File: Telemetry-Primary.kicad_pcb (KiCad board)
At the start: 2 copper layers, 95 x 95 mm, 162 parts, among them J1 CAN_LogicAnalyzer, J10 SMAConn, J11 CAN_In, J12 CAN_Out, J13 Breakouts, J14 RTC_BATT, J2 IMU_LogicAnalyzer, J3 GPS_LogicAnalyzer, J4 SWD, J5 SDCard_LogicAnalyzer, J6 USB_B_Micro, J7 PowerConn, J8 RJ45_Abracon_ARJP11A-MASA-B-A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, J9 Micro_SD_Card_Det, Q1 Q_PMOS_GSD, SW1 Reset, SW2 RTCC_BattCheck, SW4 SW_Push, SW5 SW_Push, SW6 SW_Push, SW7 SW_Push, U1 STM32F429ZITx, U10 LAN8742A-CZ-TR, U11 USBLC6-4SC6, U2 RI3-1205S, U3 LD1117-3.3_SOT223, U4 ADM3055E, U5 CDSOT23-T24CAN, U6 BNO055, U7 MTK3339, U8 CP2102N-A02-GQFN24, U9 BLUENRG-M2SA, Y1 8M, Y2 25M, Y3 32.768k

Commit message: layout changes, telemetryCAN added, IMU removed
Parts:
- removed R1, R2: 4.7k, Resistor_SMD:R_0805_2012Metric
- removed R30: 10k, Resistor_SMD:R_0805_2012Metric
- added C65: 10u, Capacitor_SMD:C_0805_2012Metric, B.Cu at (150.4, 71.3)
- added C66: 0.1u, Capacitor_SMD:C_0805_2012Metric, B.Cu at (150.4, 68.8)
- added C67: 0.1u, Capacitor_SMD:C_0805_2012Metric, B.Cu at (150.4, 66.3)
- added C68: 0.01u, Capacitor_SMD:C_0805_2012Metric, B.Cu at (150.4, 63.9)
- added J15: CAN_Out, UTSVT_Connectors:Molex_MicroFit3.0_1x4xP3.00mm_PolarizingPeg_Vertical, F.Cu at (155.3, 49.4)
- added L3: 2k, Inductor_SMD:L_0805_2012Metric, F.Cu at (150.2, 52.7)
- added L4: 2k, Inductor_SMD:L_0805_2012Metric, F.Cu at (150.1, 57.3)
- added TP8: CAN_H, TestPoint:TestPoint_Keystone_5005-5009_Compact, F.Cu at (167.0, 60.5)
- added TP9: CAN_L, TestPoint:TestPoint_Keystone_5005-5009_Compact, F.Cu at (167.0, 54.9)
- added U12: ADM3055E, UTSVT_ICs:SOIC-20W_7.5x15.4mm_Pitch1.27mm, F.Cu at (154.6, 64.5)
- C36: value 6.8n -> 0.22u
- C37: value 120n -> 10u
- C39: value 0.1u -> 0.01u
- C42, C43, C44, C45, R35: moved to B.Cu
- J13: footprint Connector_PinHeader_2.54mm:PinHeader_1x06_P2.54mm_Vertical -> Connector_Molex:Molex_Micro-Fit_3.0_43045-0612_2x03_P3.00mm_Vertical
- J2: value IMU_LogicAnalyzer -> CAN_LogicAnalyzer; footprint Connector_PinHeader_2.54mm:PinHeader_1x05_P2.54mm_Vertical -> Connector_PinHeader_2.54mm:PinHeader_1x03_P2.54mm_Vertical
- LOGO2: moved to F.Cu
- R28: value 10k -> 0
- R29: value 10k -> 120; moved to B.Cu
- U6: value BNO055 -> CDSOT23-T24CAN; footprint Package_LGA:LGA-28_5.2x3.8mm_P0.5mm -> Package_TO_SOT_SMD:SOT-23W
- moved H2 117.2 mm to (181.3, 134.9)
- moved J10 83.7 mm to (111.6, 132.5), turned to 90 degrees
- moved U7 77.2 mm to (161.8, 127.6), turned to -90 degrees
- moved U9 68.9 mm to (177.2, 52.9), turned to -90 degrees
- moved C63 67.3 mm to (172.8, 48.3), turned to -90 degrees
- moved D4 67.0 mm to (151.3, 128.4), turned to 90 degrees
- moved R31 65.0 mm to (178.8, 63.4), turned to 180 degrees
- moved C62 63.9 mm to (169.7, 48.3), turned to -90 degrees
- moved R27 63.3 mm to (151.3, 124.4)
- moved C51 59.8 mm to (174.9, 63.4), turned to 180 degrees
- moved R3 56.6 mm to (116.0, 87.2), turned to 0 degrees
- moved D2 55.3 mm to (116.0, 89.6), turned to 180 degrees
- moved R34 54.5 mm to (144.3, 57.3), turned to 0 degrees
- moved TP7 53.6 mm to (127.1, 63.2)
- moved U5 53.2 mm to (139.1, 54.7), turned to 90 degrees
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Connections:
- net /CAN/CAN_H renamed /CarCAN/CAN_H
- net /CAN/CAN_L renamed /CarCAN/CAN_L
- net /CAN/RSlope renamed /CarCAN/RSlope
- net /USART7_TX renamed /USART6_RX
- C36 pad 1: +3.3V -> Net-(U12-V_ISO_Out)
- C36 pad 2: GND -> Net-(C36-Pad2)
- C37 pad 1: +3.3V -> Net-(J15-5V)
- C37 pad 2: GND -> Net-(J15-GND)
- C38 pad 1: GND -> Net-(J15-5V)
- C38 pad 2: Net-(U6-CAP) -> Net-(J15-GND)
- C39 pad 1: +3.3V -> Net-(J15-5V)
- C39 pad 2: GND -> Net-(J15-GND)
- J13 pad 2: /SPI3_CLK -> /SPI3_MISO
- J13 pad 3: /SPI3_MISO -> /PD0
- J13 pad 4: /SPI3_MOSI -> /SPI3_CLK
- J13 pad 5: /PD0 -> /SPI3_MOSI
- J2 pad 2: /I2C1_SCL -> /CAN2_TX
- J2 pad 3: /I2C1_SDA -> /CAN2_RX
- J3 pad 2: /USART2_TX -> /USART3_TX
- J3 pad 3: /USART2_RX -> /USART3_RX
- J3 pad 4: /PD7 -> /PD10
- J3 pad 5: /PG9 -> /PD11
- R27 pad 1: /PD7 -> /PD10
- R28 pad 1: +3.3V -> /TelemetryCAN/RSlope
- R28 pad 2: /PB5 -> Net-(J15-GND)
- R29 pad 1: GND -> /TelemetryCAN/CAN_H
- R29 pad 2: Net-(U6-COM3) -> /TelemetryCAN/CAN_L
- U1 pad 135: /PB5 -> /CAN2_RX
- U1 pad 136: /I2C1_SCL -> /CAN2_TX
- U1 pad 137: /I2C1_SDA -> /PB7
- U6 pad 1: unconnected-(U6-PIN1-Pad1) -> /TelemetryCAN/CAN_H
- U6 pad 2: GND -> /TelemetryCAN/CAN_L
- U6 pad 3: +3.3V -> Net-(J15-GND)
- U7 pad 10: /USART2_TX -> /USART3_TX
- U7 pad 13: /PG9 -> /PD11
- U7 pad 5: /PD7 -> /PD10
- U7 pad 9: /USART2_RX -> /USART3_RX
- U9 pad 10: /USART3_RX -> /USART2_RX
- U9 pad 11: /USART3_TX -> /USART2_TX
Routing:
- net +BATT: track 48.6 -> 154.8 mm, vias 1 -> 2
- net /PD11: track 0.00 -> 53.9 mm
- net /PD10: track 0.00 -> 47.1 mm
- net +3.3V: track 382.4 -> 342.0 mm
- net /PG9: track 36.7 -> 0.00 mm
- net Net-(J15-GND): track 0.00 -> 36.1 mm
- net /TelemetryCAN/CAN_H: track 0.00 -> 33.8 mm
- net /PD7: track 29.0 -> 0.00 mm
- net /I2C1_SCL: track 28.3 -> 0.00 mm, vias 2 -> 0
- net /PB4: track 26.7 -> 0.00 mm, vias 2 -> 0
- net /I2C1_SDA: track 24.7 -> 0.00 mm, vias 2 -> 0
- net /PB5: track 24.1 -> 0.00 mm, vias 2 -> 0
- net /CarCAN/CAN_L: track 70.1 -> 47.3 mm, vias 2 -> 0
- net /TelemetryCAN/CAN_L: track 0.00 -> 22.8 mm
- net Net-(J10-In): track 23.3 -> 45.6 mm
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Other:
- board size 95 x 95 mm -> 77.5 x 91.8 mm
- board text added: "+"
- board text added: "D10"
- board text added: "D11"
- board text added: "Jump if end of CarCAN"
- board text added: "RTC Check"
- board text added: "UTSVT - Telemetry Leader v3.0 Summer 2023 -Design by Sijin Woo, Chase Block, Andrew Nguyen"
- board text removed: "B4"
- board text removed: "B5"
- board text removed: "D7"
- board text removed: "G9"
- board text removed: "RTC Battery Check"
- board text removed: "SCL"
- board text removed: "SDA"
- board text removed: "UTSVT - Telemetry Leader v2.2 Summer 2023 Design by Sijin Woo and Chase Block"

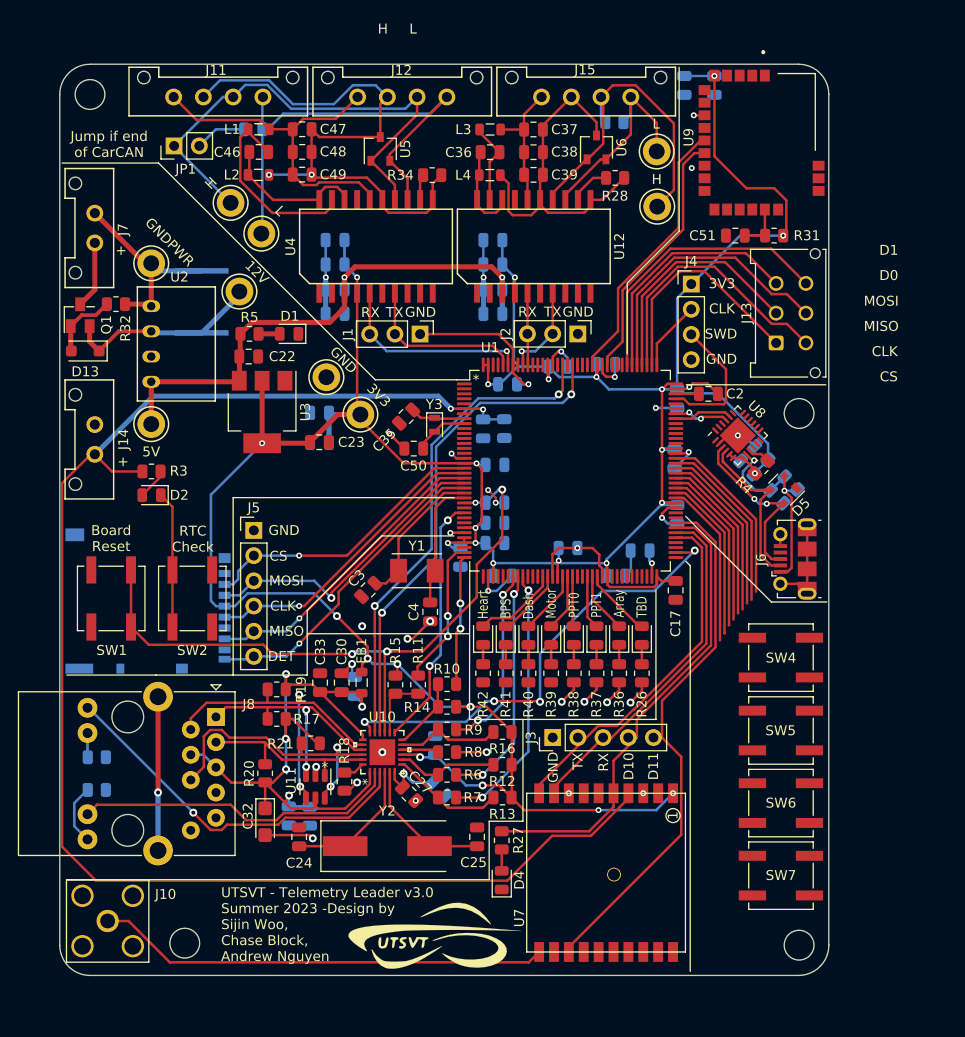
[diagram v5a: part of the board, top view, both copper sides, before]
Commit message: inputs routing + fixed models + clock keepouts
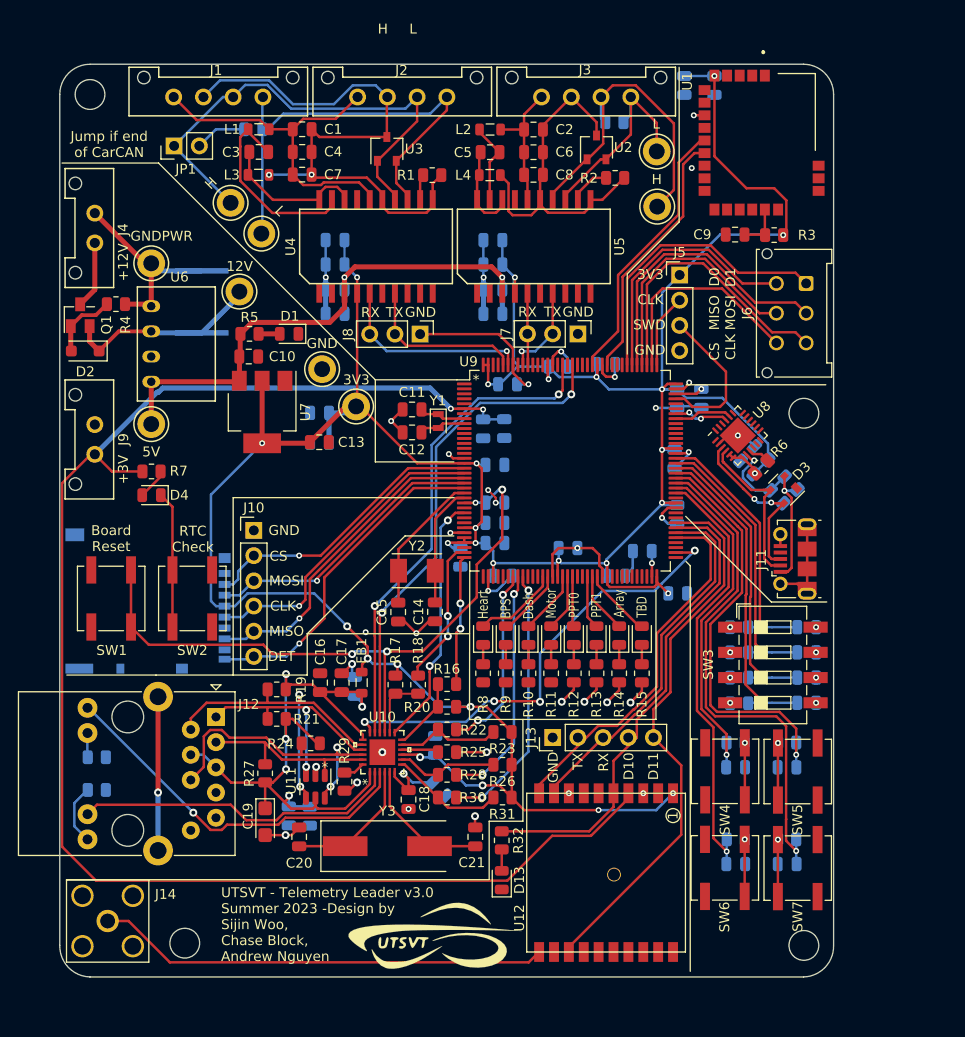
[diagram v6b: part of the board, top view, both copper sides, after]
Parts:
- added C56: .1u, Capacitor_SMD:C_0805_2012Metric, B.Cu at (182.1, 102.9)
- added C57: .1u, Capacitor_SMD:C_0805_2012Metric, B.Cu at (182.1, 105.4)
- added C58: .1u, Capacitor_SMD:C_0805_2012Metric, B.Cu at (182.1, 108.0)
- added C60: .1u, Capacitor_SMD:C_0805_2012Metric, B.Cu at (182.1, 110.5)
- added C62: .1u, Capacitor_SMD:C_0805_2012Metric, B.Cu at (180.1, 117.0)
- added C63: .1u, Capacitor_SMD:C_0805_2012Metric, B.Cu at (174.9, 117.0)
- added C67: .1u, Capacitor_SMD:C_0805_2012Metric, B.Cu at (180.1, 126.7)
- added C68: .1u, Capacitor_SMD:C_0805_2012Metric, B.Cu at (174.9, 126.7)
- added R37: 1k, Resistor_SMD:R_0805_2012Metric, B.Cu at (175.3, 102.9)
- added R38: 1k, Resistor_SMD:R_0805_2012Metric, B.Cu at (175.3, 105.4)
- added R39: 1k, Resistor_SMD:R_0805_2012Metric, B.Cu at (175.3, 108.0)
- added R40: 1k, Resistor_SMD:R_0805_2012Metric, B.Cu at (175.3, 110.5)
- added R41: 1k, Resistor_SMD:R_0805_2012Metric, B.Cu at (180.1, 114.5)
- added R42: 1k, Resistor_SMD:R_0805_2012Metric, B.Cu at (174.9, 114.5)
- added R45: 1k, Resistor_SMD:R_0805_2012Metric, B.Cu at (180.1, 124.3)
- added R46: 1k, Resistor_SMD:R_0805_2012Metric, B.Cu at (174.9, 124.3)
- added SW3: SW_DIP_x04, Button_Switch_SMD:SW_DIP_SPSTx04_Slide_6.7x11.72mm_W8.61mm_P2.54mm_LowProfile, F.Cu at (178.7, 106.7)
- C36: renamed from C2; moved to B.Cu
- C55: renamed from C17; moved to B.Cu
- moved SW5 11.6 mm to (181.2, 117.4), turned to -90 degrees
- moved LOGO2 9.33 mm to (157.5, 121.7)
- moved SW4 6.98 mm to (173.8, 117.4), turned to 90 degrees
- moved SW7 6.77 mm to (181.2, 127.2), turned to -90 degrees
- moved J6 6.72 mm to (182.0, 68.2), turned to -90 degrees
- moved SW6 5.71 mm to (173.8, 127.1), turned to 90 degrees
- moved C15 3.76 mm to (140.9, 101.3), turned to -90 degrees
- moved C12 1.64 mm to (142.3, 83.2)
- moved J5 1.48 mm to (169.3, 67.4)
- moved C11 0.93 mm to (142.3, 80.9), turned to 0 degrees
- moved TP8 0.92 mm to (136.7, 80.6)
- moved TP7 0.92 mm to (133.2, 76.9)
- moved C36 0.85 mm to (171.4, 79.8), turned to -90 degrees
- moved U3 0.66 mm to (139.8, 54.7)
- moved C18 0.56 mm to (141.9, 120.2), turned to 90 degrees
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- renumbered C47 to C1, C22 to C10, C35 to C11, C50 to C12, C23 to C13, C4 to C14, C3 to C15, C33 to C16, C30 to C17, C27 to C18, C32 to C19, C37 to C2, C24 to C20, C25 to C21, C63 to C22, C62 to C23, C45 to C24, C68 to C25, C44 to C26, C67 to C27, C66 to C28, C43 to C29, C46 to C3, C21 to C30, C42 to C31, C65 to C32, C13 to C33, C12 to C34, C11 to C35, C14 to C37, C60 to C38, C64 to C39, C48 to C4, C9 to C40, C61 to C41, C40 to C42, C15 to C43, C7 to C44, C41 to C45, C10 to C46, C16 to C47, C5 to C48, C6 to C49, C36 to C5, C19 to C50, C1 to C51, C8 to C52, C18 to C53, C20 to C54, C34 to C59, C38 to C6, C28 to C61, C26 to C64, C31 to C65, C29 to C66, C49 to C7, C39 to C8, C51 to C9, D7 to D10, D6 to D11, D3 to D12, D4 to D13, D13 to D2, D5 to D3, D2 to D4, D12 to D5, D11 to D6, D10 to D7, D9 to D8, D8 to D9, H3 to H2, H4 to H3, H2 to H4, J11 to J1, J5 to J10, J6 to J11, J8 to J12, J3 to J13, J10 to J14, J9 to J15, J12 to J2, J15 to J3, J7 to J4, J4 to J5, J13 to J6, J2 to J7, J1 to J8, J14 to J9, L3 to L2, L2 to L3, LOGO2 to LOGO1, LOGO1 to LOGO2, R34 to R1, R40 to R10, R39 to R11, R38 to R12, R37 to R13, R36 to R14, R26 to R15, R10 to R16, R15 to R17, R11 to R18, R28 to R2, R14 to R20, R17 to R21, R9 to R22, R16 to R23, R21 to R24, R8 to R25, R12 to R26, R20 to R27, R6 to R28, R18 to R29, R31 to R3, R7 to R30, R13 to R31, R27 to R32, R29 to R33, R35 to R34, R24 to R35, R25 to R36, R32 to R4, R23 to R43, R22 to R44, R4 to R6, R3 to R7, R42 to R8, R41 to R9, SW5 to SW4, SW4 to SW5, SW7 to SW6, SW6 to SW7, TP9 to TP1, TP6 to TP2, TP8 to TP3, TP7 to TP4, TP2 to TP5, TP1 to TP6, TP4 to TP7, TP5 to TP8, TP3 to TP9, U9 to U1, U7 to U12, U6 to U2, U5 to U3, U12 to U5, U2 to U6, U3 to U7, U1 to U9, Y3 to Y1, Y1 to Y2, Y2 to Y3
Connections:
- J6 pad 1: /SPI3_CS -> /PD1
- J6 pad 2: /SPI3_MISO -> /SPI3_MOSI
- J6 pad 3: /PD0 -> /SPI3_CLK
- J6 pad 4: /SPI3_CLK -> /PD0
- J6 pad 5: /SPI3_MOSI -> /SPI3_MISO
- J6 pad 6: /PD1 -> /SPI3_CS
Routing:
- net /PG3: track 16.9 -> 51.6 mm, vias 0 -> 1
- net /PD15: track 16.7 -> 44.0 mm, vias 0 -> 1
- net /PG4: track 17.0 -> 42.6 mm, vias 0 -> 1
- net /PG2: track 16.7 -> 34.8 mm, vias 0 -> 1
- net /PD14: track 16.7 -> 0.00 mm
- net /PG5: track 17.4 -> 32.7 mm, vias 0 -> 1
- net /PG6: track 17.6 -> 30.7 mm, vias 0 -> 1
- net /PG7: track 18.0 -> 28.7 mm, vias 0 -> 1
- net /PG8: track 17.9 -> 26.7 mm, vias 0 -> 1
- net Net-(R42-Pad2): track 0.00 -> 5.75 mm, vias 0 -> 1
- net Net-(R41-Pad2): track 0.00 -> 5.75 mm, vias 0 -> 1
- net Net-(R40-Pad2): track 0.00 -> 5.75 mm, vias 0 -> 1
- net Net-(R39-Pad2): track 0.00 -> 5.75 mm, vias 0 -> 1
- net GND: track 120.6 -> 124.9 mm, vias 35 -> 39
- net /PD11: track 53.9 -> 56.0 mm
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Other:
- board size 77.5 x 91.8 mm -> 78 x 92 mm
- board text added: "+12V"
- board text added: "+3V"
- board text removed: "+"

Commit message: silk screen cleanup + comments
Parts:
- moved C35 2.02 mm to (150.7, 76.8)
- moved C40 1.93 mm to (150.7, 84.4), turned to 0 degrees
- moved JP1 1.71 mm to (119.2, 55.8)
- moved C39 1.12 mm to (150.6, 82.2), turned to 0 degrees
- moved C33 0.41 mm to (161.8, 76.8)
- moved C50 0.30 mm to (158.0, 95.2)
- moved C43 0.26 mm to (169.0, 86.0)
- moved C34 0.15 mm to (157.0, 76.8)
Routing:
- net /CarCAN/CAN_L: track 46.7 -> 50.3 mm
- net +3.3V: track 343.9 -> 345.8 mm
- net Net-(J1-GND): track 60.7 -> 60.1 mm
- net /CarCAN/CAN_H: track 49.4 -> 48.9 mm
